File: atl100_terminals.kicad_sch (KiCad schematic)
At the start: 17 parts, among them J1 Conn_01x04_Pin, J2 Screw_Terminal_01x02, J3 Screw_Terminal_01x02, J4 Screw_Terminal_01x02, J5 Screw_Terminal_01x02, J6 Screw_Terminal_01x04, J7 Screw_Terminal_01x04, J8 Screw_Terminal_01x06

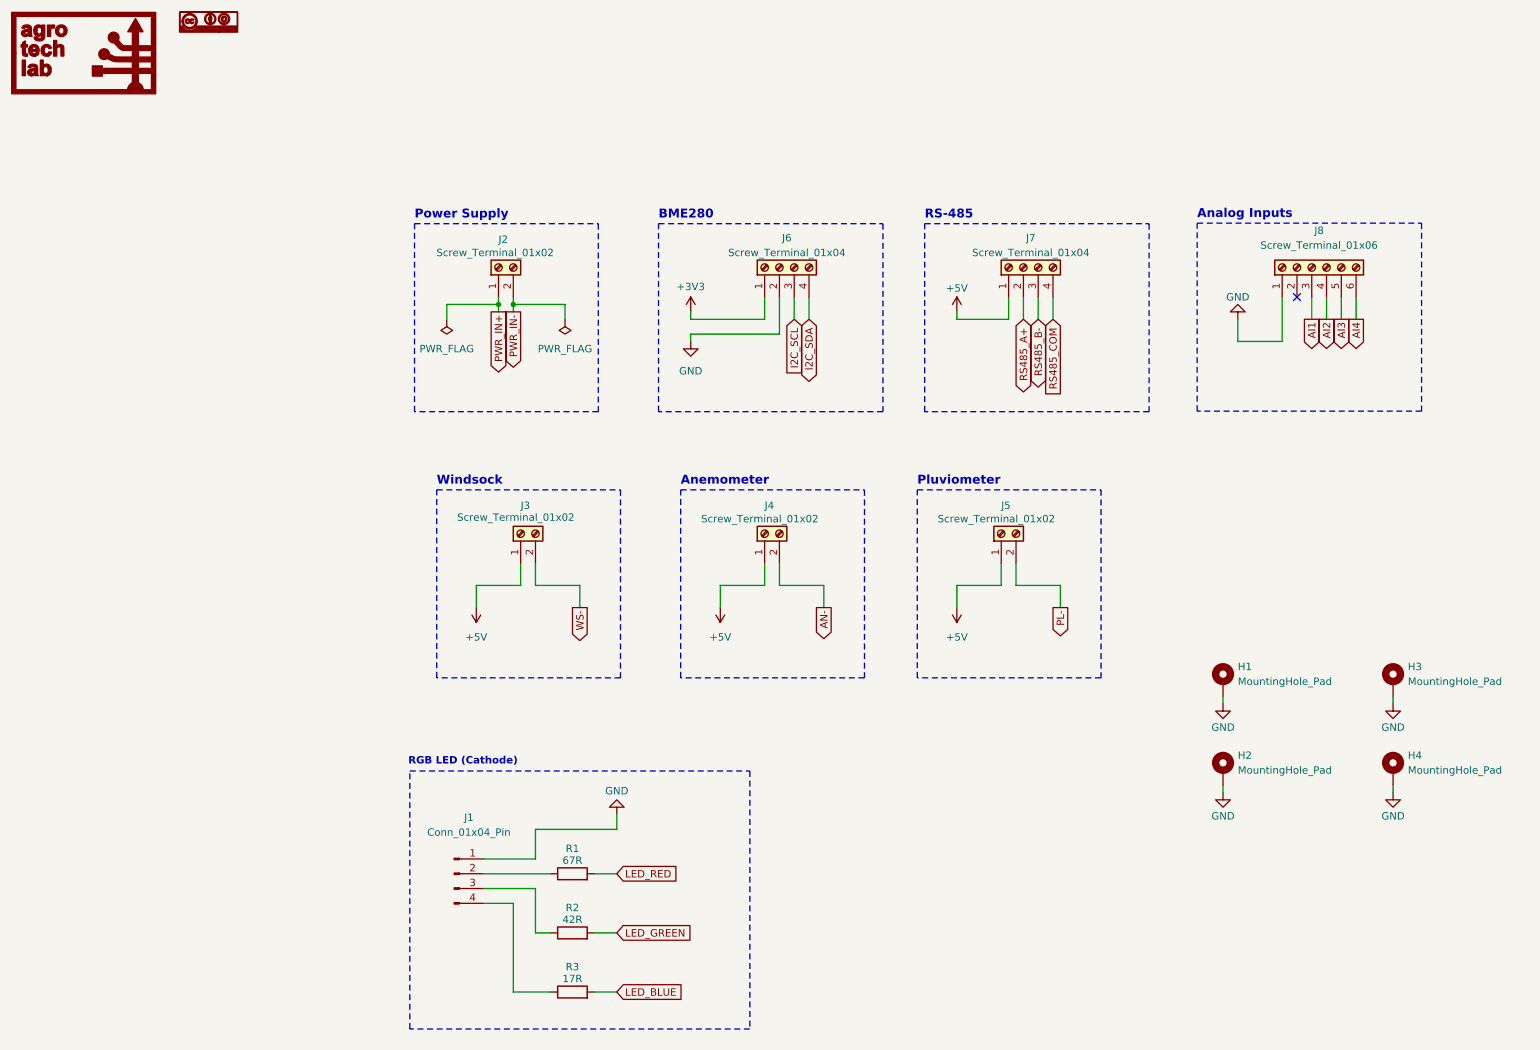
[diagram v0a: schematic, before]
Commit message: feat: Main board schematic updated
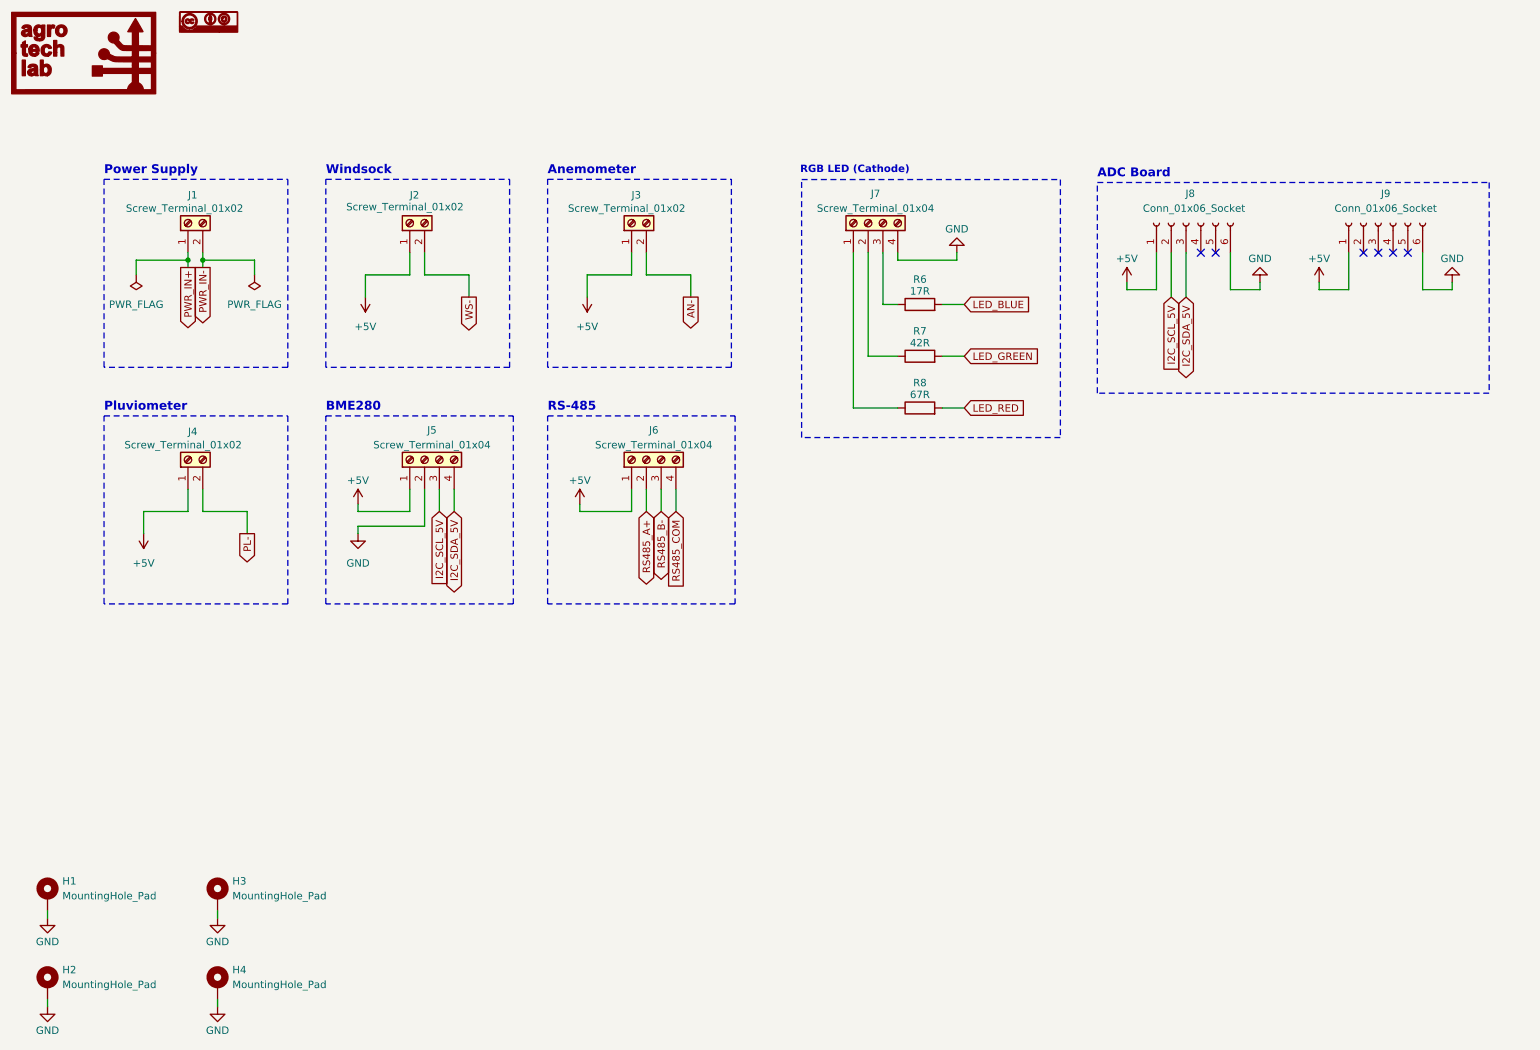
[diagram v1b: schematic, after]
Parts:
- removed J1: Conn_01x04_Pin, Connector_PinHeader_2.54mm:PinHeader_1x04_P2.54mm_Vertical, symbol Connector:Conn_01x04_Pin
- removed J8: Screw_Terminal_01x06, TerminalBlock_Phoenix:TerminalBlock_Phoenix_MKDS-1,5-6-5.08_1x06_P5.08mm_Horizontal, symbol Connector:Screw_Terminal_01x06
- added J7: Screw_Terminal_01x04, TerminalBlock_Phoenix:TerminalBlock_Phoenix_MKDS-1,5-4-5.08_1x04_P5.08mm_Horizontal, symbol Connector:Screw_Terminal_01x04
- added J8, J9: Conn_01x06_Socket, Connector_PinSocket_2.54mm:PinSocket_1x06_P2.54mm_Vertical, symbol Connector:Conn_01x06_Socket
- renumbered J2 to J1, J3 to J2, J4 to J3, J5 to J4, J6 to J5, J7 to J6, R3 to R6, R2 to R7, R1 to R8, U7 to U1, U5 to U2
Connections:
- net +3V3 is gone; now on net +5V: J5.1 (Pin_1)
- net +5V: now also J8.1 (Pin_1), J9.1 (Pin_1)
- net GND: now also J7.4 (Pin_4), J8.6 (Pin_6), J9.6 (Pin_6)
- net at R6.1: now also J7.3 (Pin_3)
- net at R7.1: now also J7.2 (Pin_2)
- net at R8.1: now also J7.1 (Pin_1)
- net I2C_SCL renamed I2C_SCL_5V
- net I2C_SCL_5V: now also J8.2 (Pin_2)
- net I2C_SDA renamed I2C_SDA_5V
- net I2C_SDA_5V: now also J8.3 (Pin_3)
- no-connect marks 1 -> 6
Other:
- note added: "ADC Board"
- note removed: "Analog Inputs"
- title: ATL-100 (Multiparametric Station) -> ATL-100 (Multiparametric Station) - Main Board
- moved on the sheet: H1, H2, H3, H4, J1, J2, J3, J4, J5, J6, R6, R7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

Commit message: feat: Updated to v0.2.0
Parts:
- removed J7: Screw_Terminal_01x04, TerminalBlock_Phoenix:TerminalBlock_Phoenix_MKDS-1,5-4-5.08_1x04_P5.08mm_Horizontal, symbol Connector:Screw_Terminal_01x04
- removed U1: ~, AgroTechLab:Logo AgroTechLab, symbol AgroTechLab:Logo - AgroTechLab
- removed U2: ~, AgroTechLab:Logo CC-BY-SA, symbol AgroTechLab:Logo - CC-BY-SA
- added J7: Conn_01x04_Pin, Connector_PinHeader_2.54mm:PinHeader_1x04_P2.54mm_Horizontal, symbol Connector:Conn_01x04_Pin
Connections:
- net +5V: now also J6.4 (Pin_4); no longer J6.1 (Pin_1)
- net GND: now also J7.1 (Pin_1)
- net I2C_SCL_5V: now also J5.4 (Pin_4); no longer J5.3 (Pin_3)
- net I2C_SDA_5V: now also J5.3 (Pin_3); no longer J5.4 (Pin_4)
- net RS485_A+: now also J6.3 (Pin_3); no longer J6.2 (Pin_2)
- net RS485_B-: now also J6.2 (Pin_2); no longer J6.3 (Pin_3)
- net RS485_COM: now also J6.1 (Pin_1); no longer J6.4 (Pin_4)
- net at R6.1: now also J7.2 (Pin_2)
- net at R7.1: now also J7.3 (Pin_3)
- net at R8.1: now also J7.4 (Pin_4)
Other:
- moved on the sheet: J6
